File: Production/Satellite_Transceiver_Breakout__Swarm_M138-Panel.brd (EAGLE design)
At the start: 35.6 x 88.9 mm, 98 parts, among them Q2 20V/4.2A/52mΩ/1.4W, Q4 20V/4.2A/52mΩ/1.4W, U1 CH340E_MSOP10, U2 SWARM_M138_TRANSCEIVER_MAIN, U3 3.3V

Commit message: Adds production files
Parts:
- removed FRAME1: FRAME-LEDGER, SparkFun-Aesthetics:CREATIVE_COMMONS
- added BYP1, BYP2, BYP3: JUMPER-SMT_2_NO_SILK, SparkFun-Jumpers:SMT-JUMPER_2_NO_SILK
- added C11, C12, C13, C15, C16, C21, C22, C23, C25, C26, C31, C32, C33, C35, C36: 0.1uF, SparkFun-Capacitors:0603
- added C14, C24, C34: 10uF, SparkFun-Capacitors:0603
- added C17, C27, C37: 10nF, SparkFun-Capacitors:0603
- added C18, C19, C28, C29, C38, C39: 100uF, SparkFun-Capacitors:PANASONIC_D
- added C20, C30, C40: 1.0uF, SparkFun-Capacitors:0603
- added D10, D4, D7: PRTR5V0U2F, SparkFun-IC-Power:SOT886
- added D11, D5, D8: GREEN, SparkFun-LED:LED-0603
- added D12, D6, D9: Yellow, SparkFun-LED:LED-0603
- added E$1, E$2, E$3, E$4: (no value), SparkFun-Aesthetics:FIDUCIAL-1X2
- added E$5, E$6: (no value), SparkFun-Retired:FIDUCIAL-1.5X3
- added E3, E5, E7: VHF, SparkFun-RF:SMA-EDGE
- added E4, E6, E8: GPS, SparkFun-RF:SMA-EDGE
- added F2, F3, F4: 6V/2A, SparkFun-Fuses:1210
- added FD10, FD11, FD12, FD13, FD14, FD15, FD16, FD5, FD6, FD7, FD8, FD9: FIDUCIAL1X2, SparkFun-Aesthetics:FIDUCIAL-1X2
- added GPIO2, GPIO3, GPIO4: JUMPER-SMT_3_1-NC_TRACE_SILK, SparkFun-Jumpers:SMT-JUMPER_3_1-NC_TRACE_SILK
- added GPS1, GPS2, GPS3, VHF1, VHF2, VHF3: U.FL, SparkFun-Connectors:U.FL
- added H10, H13, H14, H15, H16, H19, H20, H21, H22, H7, H8, H9: STAND-OFF, SparkFun-Hardware:STAND-OFF
- added H11, H12, H17, H18, H23, H24: STAND-OFF-REFLOW-M2.5_1.5MM_TALL, SparkFun-Hardware:STAND-OFF-REFLOW-M2.5
- added J3, J5, J7: (no value), SparkFun-Connectors:USB-C-16P-2LAYER-PADS
- added J4, J6, J8: (no value), SparkFun-Connectors:1X04_NO_SILK
- added JP2, JP3, JP4: USB_SOLDER_PADS, SparkFun-Connectors:USB-SOLDER-PADS
- added LOGO10, LOGO7: OSHW-LOGOM, SparkFun-Aesthetics:OSHW-LOGO-M
- added LOGO11, LOGO12, LOGO5, LOGO6, LOGO8, LOGO9: SFE_LOGO_NAME_FLAME.1_INCH, SparkFun-Aesthetics:SFE_LOGO_NAME_FLAME_.1
- added Q10, Q12, Q14, Q16, Q6, Q8: (no value), SparkFun-DiscreteSemi:SOT363_PHILIPS
- added Q11, Q13, Q15, Q5, Q7, Q9: 20V/4.2A/52mΩ/1.4W, SparkFun-DiscreteSemi:SOT23-3
- added R10, R12, R20, R26, R34, R36: 1M, SparkFun-Resistors:0603
- added R11, R15, R16, R19, R25, R29, R30, R33, R35, R39, R40, R9: 100k, SparkFun-Resistors:0603
- added R13, R27, R37: 1k, SparkFun-Resistors:0603
- added R14, R28, R38: 2.2k, SparkFun-Resistors:0603
- added R17, R18, R31, R32, R7, R8: 5.1k, SparkFun-Resistors:0603
- added RXI1, RXI2, RXI3, TXO1, TXO2, TXO3: JUMPER-COMBO_2_NC_TRACE, SparkFun-Jumpers:COMBO-JUMPER_2_NC_TRACE
- added RX_LED1, RX_LED2, RX_LED3, SHLD1, SHLD2, SHLD3, TX_LED1, TX_LED2, TX_LED3: JUMPER-SMT_2_NC_TRACE_SILK, SparkFun-Jumpers:SMT-JUMPER_2_NC_TRACE_SILK
- added U$100, U$137, U$63: (no value), output:G3
- added U$101, U$138, U$64: (no value), output:D#2
- added U$102, U$139, U$65: (no value), output:D#1
- added U$103, U$104, U$140, U$141, U$66, U$67: (no value), output:SATELLITE_TRANSCEIVER_BREAKOUT0
- added U$105, U$106, U$142, U$143, U$68, U$69: (no value), output:SWARM_M1381
- added U$107, U$144, U$70: (no value), output:PLEASE_CONSULT_THE_DOCUMENTATION0
- added U$108, U$145, U$71: (no value), output:FOR_THE_PEAK_TRANSMIT_CURRENT1
- added U$109, U$146, U$72: (no value), output:NOT_COMPATIBLE_WITH_USB_2#02
- added U$110, U$147, U$73: (no value), output:VIN#__3#0V_MIN__5#0V_MAX0
- added U$111, U$148, U$74: (no value), top:#SHLD#14
- added U$112, U$2, U$75: (no value), output:VHF0
- added U$113, U$33, U$76: (no value), output:GPS0
- added U$114, U$115, U$35, U$38, U$77, U$78: (no value), output:#VIN#0
- added U$116, U$117, U$42, U$43, U$79, U$80: (no value), output:#GND#0
- added U$118, U$44, U$81: (no value), output:TX0
- added U$119, U$45, U$82: (no value), output:RX0
- added U$120, U$46, U$83: (no value), output:#TX_LED#0
- added U$121, U$47, U$84: (no value), output:#RX_LED#0
- added U$122, U$48, U$85: (no value), output:#BYPASS#0
- added U$123, U$49, U$86: (no value), output:#CH340_RXI#0
- added U$124, U$50, U$87: (no value), output:#CH340_RXI#341
- added U$125, U$51, U$88: (no value), output:#TXO#341
- added U$126, U$52, U$89: (no value), output:#TXO#342
- added U$127, U$53, U$90: (no value), output:#CH340_TXO#0
- added U$128, U$54, U$91: (no value), output:#CH340_TXO#341
- added U$129, U$55, U$92: (no value), output:#RXI#0
- added U$130, U$56, U$93: (no value), output:#RXI#1
- added U$131, U$57, U$94: (no value), output:#TX##RX##0
- added U$132, U$58, U$95: (no value), output:#TX##RX##1
- added U$133, U$59, U$96: (no value), output:#GPIO1#0
- added U$134, U$60, U$97: (no value), output:#GPIO1_#2
- added U$135, U$61, U$98: (no value), output:#_GPIO1#2
- added U$136, U$62, U$99: (no value), output:V0
- added U10, U4, U7: CH340E_MSOP10, SparkFun-IC-Comms:MSOP10
- added U11, U5, U8: SWARM_M138_TRANSCEIVER_MAIN, SparkFun-RF:M.2-SWARM-M138-A
- added U12, U6, U9: 3.3V, SparkFun-IC-Power:SOT23-5
- added VCC1, VCC2, VCC3: TEST-POINT3X5, SparkFun-Connectors:PAD.03X.05
- LOGO1: value SPECIAL_INSTRUCTIONS-ORDERING -> OSHW-LOGOM; device SparkFun-Aesthetics:ORDERING_INSTRUCTIONS -> SparkFun-Aesthetics:OSHW-LOGO-M
- moved LOGO1 112.6 mm to (53.8, 69.8)
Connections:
- new net 3.3V1: C20.1, R15.2, U6.5
- new net 3.3V2: C30.1, R29.2, U9.5
- new net 3.3V3: C40.1, R39.2, U12.5
- new net CH340_RXI1: D5.C, TXO1.2, TXO1.4, U4.9
- new net CH340_RXI2: D8.C, TXO2.2, TXO2.4, U7.9
- new net CH340_RXI3: D11.C, TXO3.2, TXO3.4, U10.9
- new net CH340_TXO1: D6.C, RXI1.1, RXI1.3, U4.8
- new net CH340_TXO2: D9.C, RXI2.1, RXI2.3, U7.8
- new net CH340_TXO3: D12.C, RXI3.1, RXI3.3, U10.8
- new net D+1: D4.6, U4.1
- new net D+2: D7.6, U7.1
- new net D+3: D10.6, U10.1
- new net D+_IN1: D4.1, J3.A6, J3.B6, JP2.D+
- new net D+_IN2: D7.1, J5.A6, J5.B6, JP3.D+
- new net D+_IN3: D10.1, J7.A6, J7.B6, JP4.D+
- new net D-1: D4.4, U4.2
- new net D-2: D7.4, U7.2
- new net D-3: D10.4, U10.2
- new net D-_IN1: D4.3, J3.A7, J3.B7, JP2.D-
- new net D-_IN2: D7.3, J5.A7, J5.B7, JP3.D-
- new net D-_IN3: D10.3, J7.A7, J7.B7, JP4.D-
- new net GND1: C11.2, C12.2, C13.2, C14.2, C15.2, C16.2, C17.2, C18.-, C19.-, C20.2, D4.2, E3.GND@0, E3.GND@1, E3.GND@2, E3.GND@3, E4.GND@0, E4.GND@1, E4.GND@2, E4.GND@3, GPS1.1, GPS1.2, H11.1, H12.1, J3.GND, J3.GND2, J4.1, JP2.GND, R10.1, R11.1, R12.1, R16.1, R7.1, R8.1, R9.1, SHLD1.1, U4.3, U5.15, U5.18, U5.21, U5.26, U5.27, U5.29, U5.34, U5.35, U5.37, U5.4, U5.40, U5.43, U5.50, U5.9, U5.A1, U5.A2, U6.2, VHF1.1, VHF1.2
- new net GND2: C21.2, C22.2, C23.2, C24.2, C25.2, C26.2, C27.2, C28.-, C29.-, C30.2, D7.2, E5.GND@0, E5.GND@1, E5.GND@2, E5.GND@3, E6.GND@0, E6.GND@1, E6.GND@2, E6.GND@3, GPS2.1, GPS2.2, H17.1, H18.1, J5.GND, J5.GND2, J6.1, JP3.GND, R17.1, R18.1, R19.1, R20.1, R25.1, R26.1, R30.1, SHLD2.1, U7.3, U8.15, U8.18, U8.21, U8.26, U8.27, U8.29, U8.34, U8.35, U8.37, U8.4, U8.40, U8.43, U8.50, U8.9, U8.A1, U8.A2, U9.2, VHF2.1, VHF2.2
- new net GND3: C31.2, C32.2, C33.2, C34.2, C35.2, C36.2, C37.2, C38.-, C39.-, C40.2, D10.2, E7.GND@0, E7.GND@1, E7.GND@2, E7.GND@3, E8.GND@0, E8.GND@1, E8.GND@2, E8.GND@3, GPS3.1, GPS3.2, H23.1, H24.1, J7.GND, J7.GND2, J8.1, JP4.GND, R31.1, R32.1, R33.1, R34.1, R35.1, R36.1, R40.1, SHLD3.1, U10.3, U11.15, U11.18, U11.21, U11.26, U11.27, U11.29, U11.34, U11.35, U11.37, U11.4, U11.40, U11.43, U11.50, U11.9, U11.A1, U11.A2, U12.2, VHF3.1, VHF3.2
- new net GPIO2: GPIO2.2, J4.3, U5.42
- new net GPIO3: GPIO3.2, J6.3, U8.42
- new net GPIO4: GPIO4.2, J8.3, U11.42
- new net GPS1: E4.SIG, GPS1.FEED
- new net GPS2: E6.SIG, GPS2.FEED
- new net GPS3: E8.SIG, GPS3.FEED
- new net N$1: J3.B5, R7.2
- new net N$11: Q5.1, Q6.3, R10.2
- new net N$17: Q8.2, Q8.5, Q8.6, R11.2
- new net N$18: Q7.1, Q8.3, R12.2
- new net N$19: C16.1, RX_LED1.1, TX_LED1.2, U4.10
- new net N$20: D5.A, R13.2
- new net N$21: D6.A, R14.2
- new net N$22: R14.1, RX_LED1.2
- new net N$23: R13.1, TX_LED1.1
- new net N$24: GPIO2.3, R15.1
- new net N$25: GPIO2.1, R16.2
- new net N$26: J5.B5, R17.2
- new net N$27: J5.A5, R18.2
- new net N$29: Q10.2, Q10.5, Q10.6, R19.2
- new net N$30: Q10.3, Q9.1, R20.2
- new net N$31: Q12.2, Q12.5, Q12.6, R25.2
- new net N$32: Q11.1, Q12.3, R26.2
- new net N$33: C26.1, RX_LED2.1, TX_LED2.2, U7.10
- new net N$34: D8.A, R27.2
- new net N$35: D9.A, R28.2
- new net N$36: R28.1, RX_LED2.2
- new net N$37: R27.1, TX_LED2.1
- new net N$38: GPIO3.3, R29.1
- new net N$39: GPIO3.1, R30.2
- new net N$4: J3.A5, R8.2
- new net N$40: J7.B5, R31.2
- new net N$41: J7.A5, R32.2
- new net N$42: Q14.2, Q14.5, Q14.6, R33.2
- new net N$43: Q13.1, Q14.3, R34.2
- new net N$44: Q16.2, Q16.5, Q16.6, R35.2
- new net N$45: Q15.1, Q16.3, R36.2
- new net N$46: C36.1, RX_LED3.1, TX_LED3.2, U10.10
- new net N$47: D11.A, R37.2
- new net N$48: D12.A, R38.2
- new net N$49: R38.1, RX_LED3.2
- new net N$50: R37.1, TX_LED3.1
- new net N$51: GPIO4.3, R39.1
- new net N$52: GPIO4.1, R40.2
- new net N$8: Q6.2, Q6.5, Q6.6, R9.2
- new net RXI1: RXI1.2, RXI1.4, U5.11
- new net RXI2: RXI2.2, RXI2.4, U8.11
- new net RXI3: RXI3.2, RXI3.4, U11.11
- new net SHLD1: J3.SHLD1, J3.SHLD2, J3.SHLD3, J3.SHLD4, SHLD1.2
- new net SHLD2: J5.SHLD1, J5.SHLD2, J5.SHLD3, J5.SHLD4, SHLD2.2
- new net SHLD3: J7.SHLD1, J7.SHLD2, J7.SHLD3, J7.SHLD4, SHLD3.2
- new net TX/!RX!1: J4.4, U5.17
- new net TX/!RX!2: J6.4, U8.17
- new net TX/!RX!3: J8.4, U11.17
- new net TXO1: TXO1.1, TXO1.3, U5.13
- new net TXO2: TXO2.1, TXO2.3, U8.13
- new net TXO3: TXO3.1, TXO3.3, U11.13
- new net VCC1: C13.1, C14.1, C15.1, C18.+, C19.+, Q5.2, Q6.4, Q7.2, Q8.4, U5.2, U5.39, U5.41, U5.52, U6.1, U6.3, VCC1.1
- new net VCC2: C23.1, C24.1, C25.1, C28.+, C29.+, Q10.4, Q11.2, Q12.4, Q9.2, U8.2, U8.39, U8.41, U8.52, U9.1, U9.3, VCC2.1
- new net VCC3: C33.1, C34.1, C35.1, C38.+, C39.+, Q13.2, Q14.4, Q15.2, Q16.4, U11.2, U11.39, U11.41, U11.52, U12.1, U12.3, VCC3.1
- new net VHF1: E3.SIG, VHF1.FEED
- new net VHF2: E5.SIG, VHF2.FEED
- new net VHF3: E7.SIG, VHF3.FEED
- new net VIN1: C12.1, J4.2, Q7.3, Q8.1
- new net VIN2: C22.1, J6.2, Q11.3, Q12.1
- new net VIN3: C32.1, J8.2, Q15.3, Q16.1
- new net V_USB1: BYP1.2, D4.5, F2.1, J3.VBUS1, J3.VBUS2, JP2.VBUS
- new net V_USB2: BYP2.2, D7.5, F3.1, J5.VBUS1, J5.VBUS2, JP3.VBUS
- new net V_USB3: BYP3.2, D10.5, F4.1, J7.VBUS1, J7.VBUS2, JP4.VBUS
- new net V_USB_1: BYP1.1, C11.1, C17.1, F2.2, Q5.3, Q6.1, U4.7
- new net V_USB_3: BYP2.1, C21.1, C27.1, F3.2, Q10.1, Q9.3, U7.7
- new net V_USB_4: BYP3.1, C31.1, C37.1, F4.2, Q13.3, Q14.1, U10.7
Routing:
- net VCC3: track 0.00 -> 84.7 mm, vias 0 -> 4
- net VCC2: track 0.00 -> 84.7 mm, vias 0 -> 4
- net VCC1: track 0.00 -> 84.7 mm, vias 0 -> 4
- net CH340_RXI1: track 0.00 -> 59.3 mm, vias 0 -> 2
- net CH340_RXI2: track 0.00 -> 59.3 mm, vias 0 -> 2
- net CH340_RXI3: track 0.00 -> 59.3 mm, vias 0 -> 2
- net CH340_TXO3: track 0.00 -> 54.8 mm, vias 0 -> 2
- net CH340_TXO2: track 0.00 -> 54.8 mm, vias 0 -> 2
- net CH340_TXO1: track 0.00 -> 54.8 mm, vias 0 -> 2
- net GPIO3: track 0.00 -> 53.7 mm, vias 0 -> 1
- net GPIO2: track 0.00 -> 53.7 mm, vias 0 -> 1
- net GPIO4: track 0.00 -> 53.7 mm, vias 0 -> 1
- net GND1: track 0.00 -> 44.3 mm, vias 0 -> 137
- net GND3: track 0.00 -> 44.3 mm, vias 0 -> 137
- net GND2: track 0.00 -> 44.3 mm, vias 0 -> 137
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- added copper zone on layer 1, net GND1
- added copper zone on layer 16, net GND1
- added copper zone on layer 1, net GND2
- added copper zone on layer 16, net GND2
- added copper zone on layer 1, net GND3
- added copper zone on layer 16, net GND3
- added copper zone on layer 1, net SHLD1
- added copper zone on layer 1, net SHLD2
- added copper zone on layer 1, net SHLD3
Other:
- board size 35.6 x 88.9 mm -> 157.5 x 118.4 mm
- board text added: "v-score"
- board text removed: "2-Layer Board 1.6mm Thickness 1oz Copper Lead-Free HASL Finish"
- board text removed: "Dimensions In Inches"
- board text removed: "Paul Clark"
- board text removed: "Revised By: Elias Santistevan"

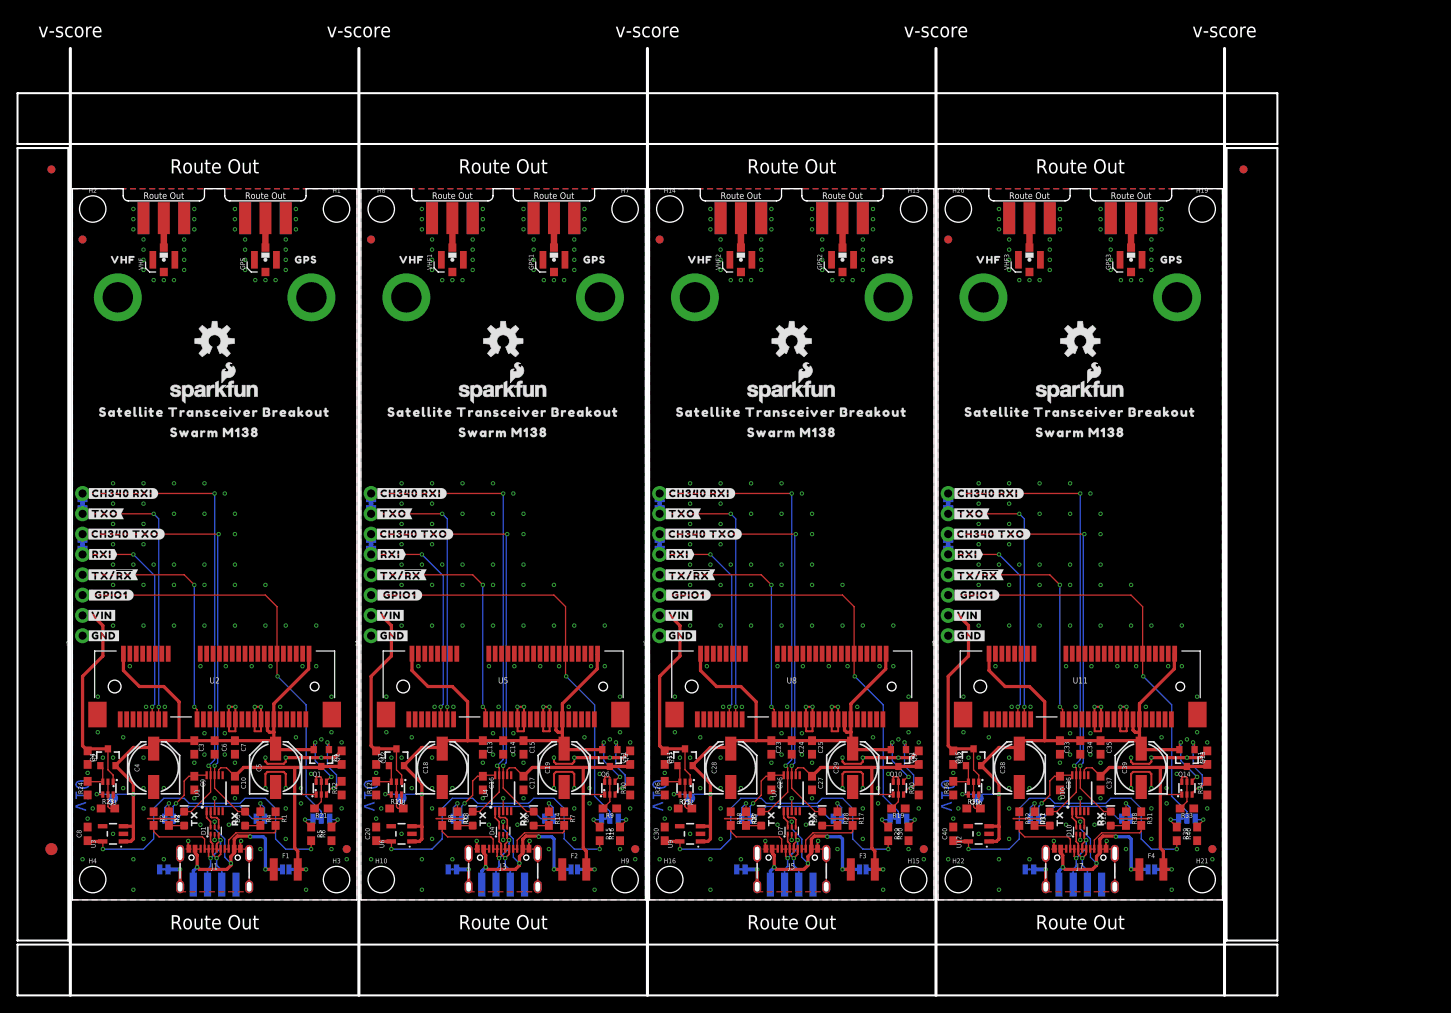
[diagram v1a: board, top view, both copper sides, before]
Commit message: Adds new panel with no vertical gaps
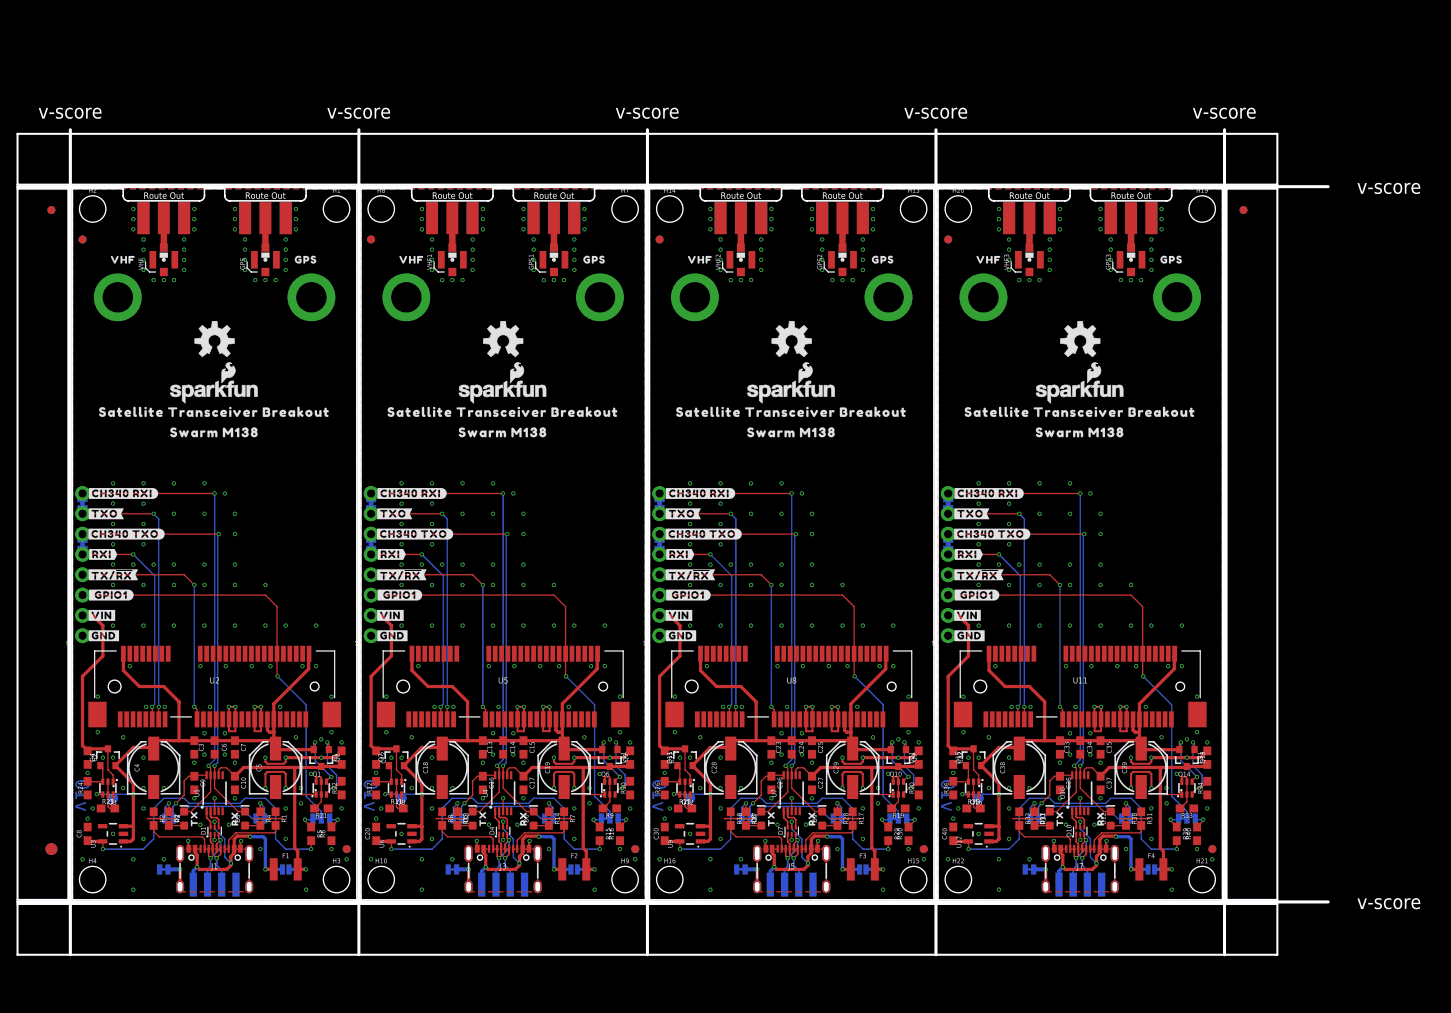
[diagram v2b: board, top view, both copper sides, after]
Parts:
- moved E$1 5.08 mm to (-2.62, 86.2)
- moved E$2 5.08 mm to (-2.62, 86.2)
- moved E$3 5.08 mm to (146.4, 86.2)
- moved E$4 5.08 mm to (146.4, 86.2)
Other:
- board size 157.5 x 118.4 mm -> 163.8 x 103.1 mm
